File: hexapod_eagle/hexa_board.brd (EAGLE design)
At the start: 80 x 90 mm, 53 parts

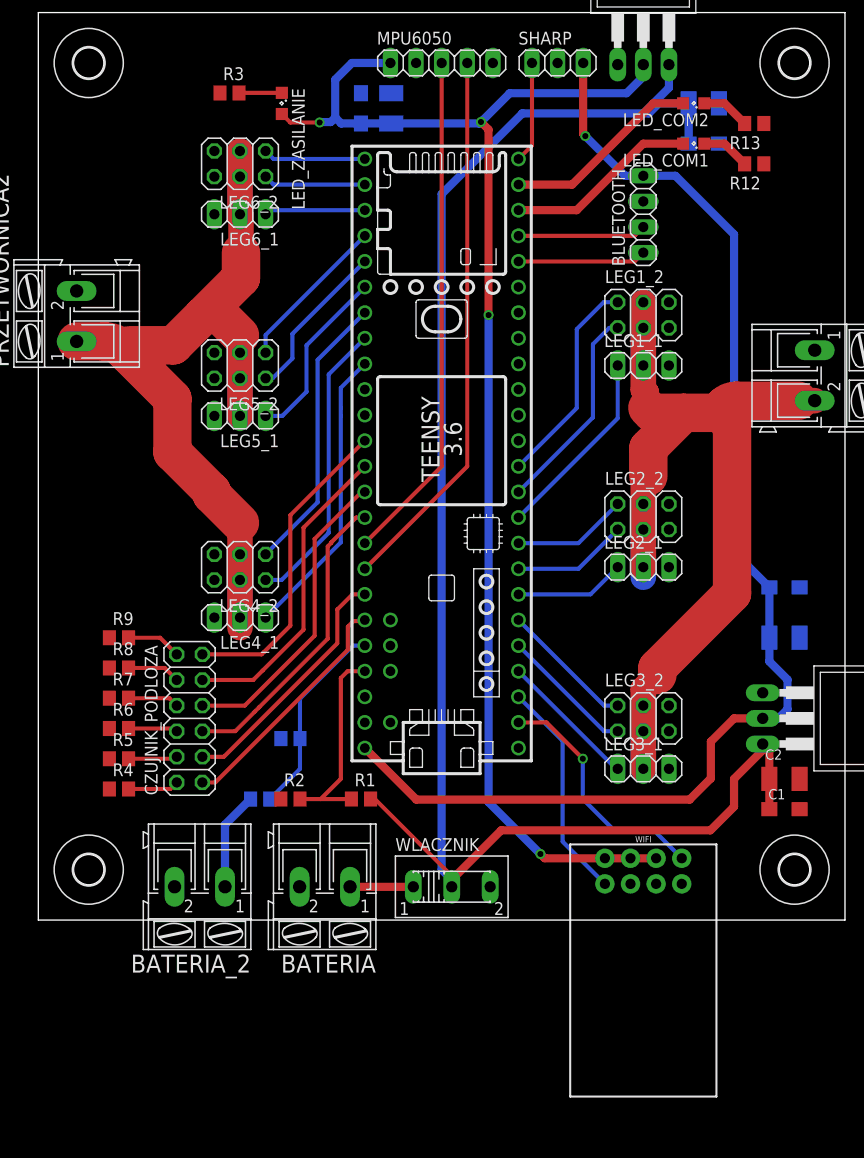
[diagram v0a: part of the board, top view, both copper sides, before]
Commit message: Update eagle files
-change to ark leg sensor pins
-change isolte value
-esp32 cam-insted bluetooth/"wifi"
-some minor changes
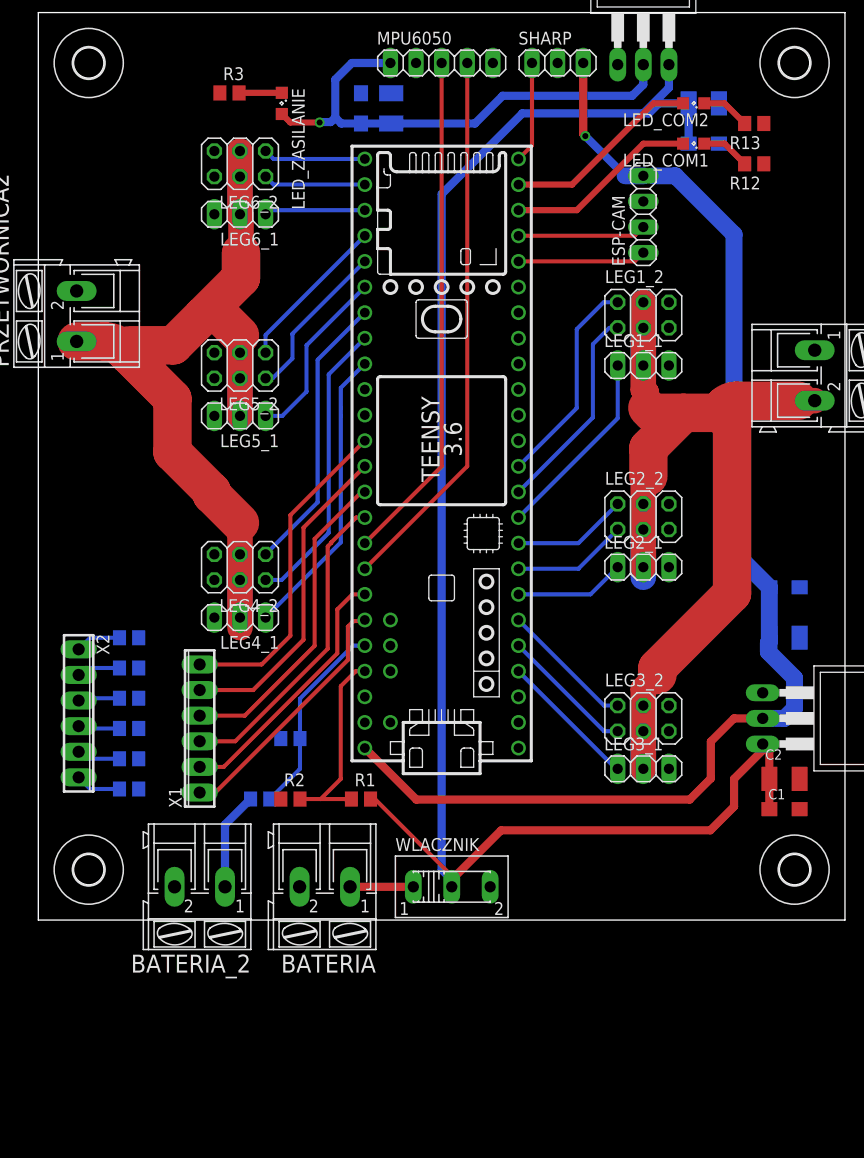
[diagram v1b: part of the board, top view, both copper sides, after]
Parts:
- removed CZUJNIK_PODLOZA: (no value), pinhead:2X06
- removed WIFI: ESP8266_ESP-01, SparkFun-RF:ESP8266_ESP-01
- added X1: ARK2, con-phoenix-254:6POL254
- added X2: ARK1, con-phoenix-254:6POL254
- BATERIA, WLACZNIK: value (none) -> 7.2V
- BATERIA_2: value (none) -> 11.1V
- ESP-CAM: value (none) -> ESP
- LED_COM1: value (none) -> YELLOW
- LED_COM2: value (none) -> RED
- LED_ZASILANIE: value (none) -> GREEN
- MPU6050: value (none) -> 6EOF
- PRZETWORNICA1, PRZETWORNICA2: value (none) -> 6V
- SHARP: value (none) -> 40CM
- moved R4 1.00 mm to (-31.0, -32.0), flipped to the bottom
- moved R5 1.00 mm to (-31.0, -29.0), flipped to the bottom
- moved R6 1.00 mm to (-31.0, -26.0), flipped to the bottom
- moved R7 1.00 mm to (-31.0, -23.0), flipped to the bottom
- moved R8 1.00 mm to (-31.0, -20.0), flipped to the bottom
- moved R9 1.00 mm to (-31.0, -17.0), flipped to the bottom
- renumbered BLUETOOTH to ESP-CAM
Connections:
- removed net INT: MPU6050.5
- removed net RXD: TEENSY41.0/RX, WIFI.1
- removed net TXD: TEENSY41.1/TX, WIFI.5
- net +3V3: no longer WIFI.2, WIFI.3, WIFI.4
- net GND: no longer WIFI.8
- net LEG1: now also X1.1; no longer CZUJNIK_PODLOZA.1
- net LEG2: now also X1.2; no longer CZUJNIK_PODLOZA.3
- net LEG3: now also X1.3; no longer CZUJNIK_PODLOZA.5
- net LEG4: now also X1.4; no longer CZUJNIK_PODLOZA.7
- net LEG5: now also X1.5; no longer CZUJNIK_PODLOZA.9
- net LEG6: now also X1.6; no longer CZUJNIK_PODLOZA.11
- net N$1: now also X2.6; no longer CZUJNIK_PODLOZA.2
- net N$2: now also X2.5; no longer CZUJNIK_PODLOZA.4
- net N$3: now also X2.4; no longer CZUJNIK_PODLOZA.6
- net N$5: now also X2.3; no longer CZUJNIK_PODLOZA.8
- net N$6: now also X2.2; no longer CZUJNIK_PODLOZA.10
- net N$7: now also X2.1; no longer CZUJNIK_PODLOZA.12
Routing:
- net +3V3: track 136.4 -> 50.1 mm, vias 4 -> 1
- net RXD: track 24.1 -> 0.00 mm, vias 1 -> 0
- net TXD: track 22.1 -> 0.00 mm
- net LEG5: track 30.8 -> 32.1 mm
- net LEG6: track 31.3 -> 32.6 mm
- net LEG3: track 30.3 -> 31.5 mm
- net LEG2: track 24.7 -> 26.0 mm
- net LEG1: track 24.1 -> 25.4 mm
- net LEG4: track 30.5 -> 31.8 mm
- net +5V: track 125.3 -> 126.3 mm
- net N$6: track 5.27 -> 4.34 mm
- net N$7: track 5.46 -> 4.53 mm
- net N$5: track 5.08 -> 4.15 mm
- net N$3: track 4.89 -> 4.15 mm
- net N$2: track 4.86 -> 4.34 mm
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
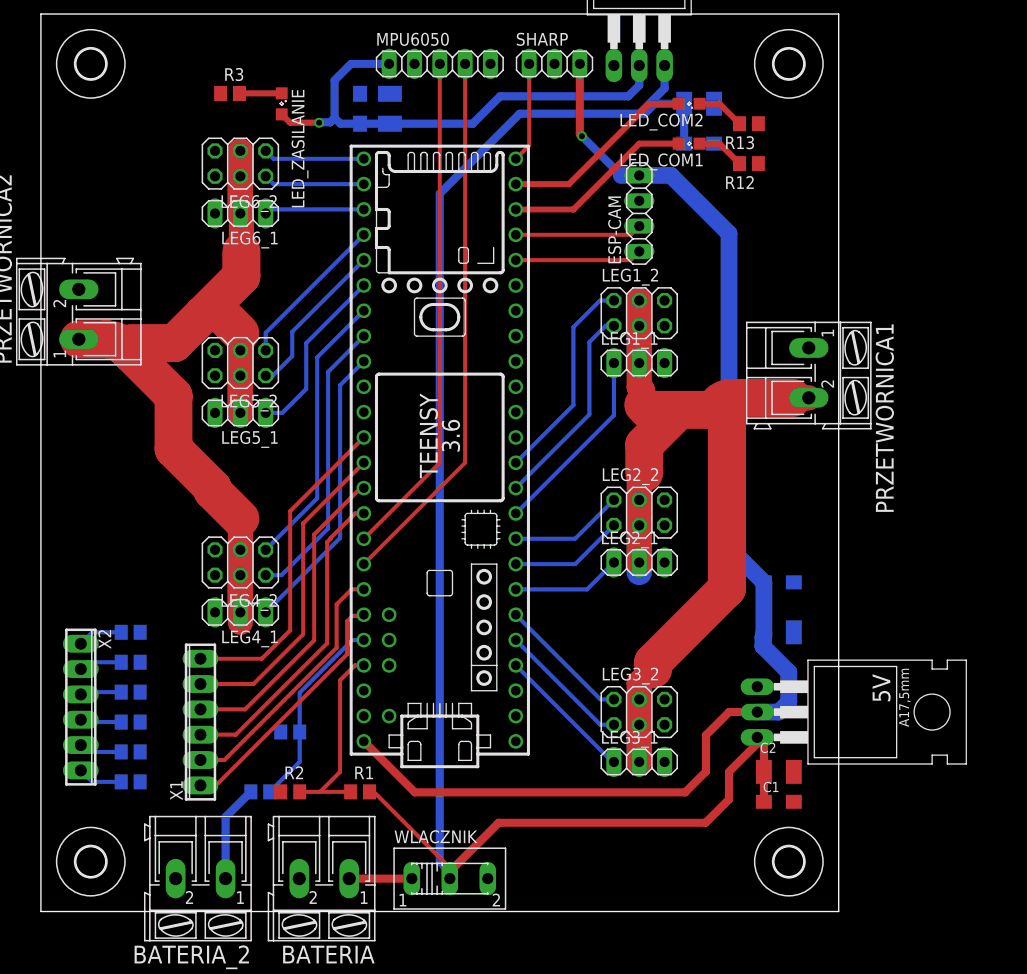
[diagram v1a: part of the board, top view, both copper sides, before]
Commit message: Update eagle schematic and board
-added capacitors
-added voltage divider
-change package some capacitors
-added on/off swich for power mcu
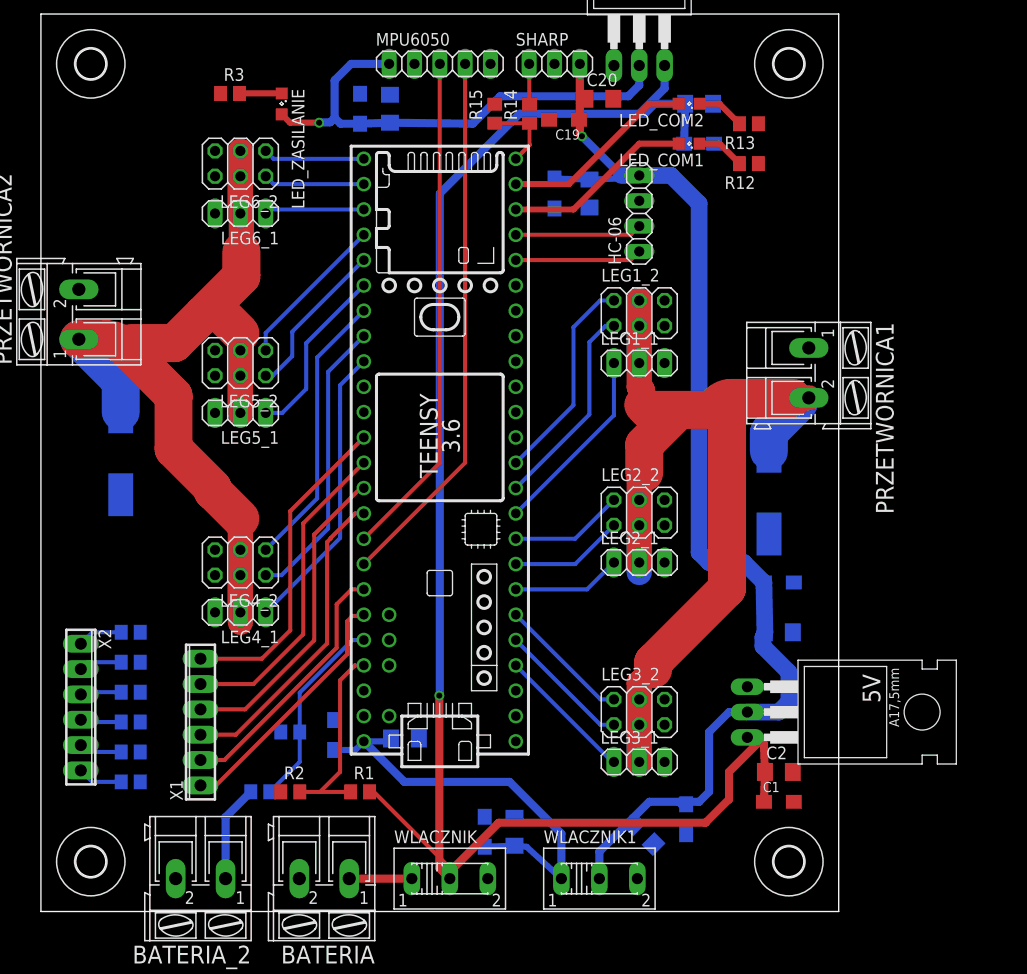
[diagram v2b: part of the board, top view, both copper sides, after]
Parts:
- added C11, C14, C15, C18, C19: 100n, rcl:SMC_A
- added C12, C13, C16, C17, C20: 10uF, rcl:C1206
- added C5, C6: (no value), rcl:150CLZ-1014
- added R14, R15: 510r, rcl:R0805
- added WLACZNIK1: 7.2V, switch:255SB
- C2, C3, C7, C8: device rcl:SMC_B -> rcl:C1206
- HC-06: value ESP -> (none)
- moved 5V 1.00 mm to (41.0, -25.0)
- renumbered ESP-CAM to HC-06
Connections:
- new net +5MCU: C11.+, C12.1, C13.1, C14.+, TEENSY41.VIN, WLACZNIK1.1
- new net N$10: R14.2, SHARP.1
- net +3V3: now also C8.1; no longer C8.+
- net +5V: now also C15.+, C16.1, C17.1, C18.+, C19.+, C20.1, C3.1, WLACZNIK1.2; no longer C3.+, TEENSY41.VIN
- net +6V1: now also C5.+
- net +6V2: now also C6.+
- net +BAT: now also C2.1, C7.1; no longer C2.+, C7.+
- net GND: now also C11.-, C12.2, C13.2, C14.-, C15.-, C16.2, C17.2, C18.-, C19.-, C2.2, C20.2, C3.2, C5.-, C6.-, C7.2, C8.2, R15.2; no longer C2.-, C3.-, C7.-, C8.-
- net SENSOR: now also R14.1, R15.1; no longer SHARP.1
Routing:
- net +5MCU: track 0.00 -> 43.2 mm
- net +6V2: track 95.6 -> 104.7 mm
- net +5V: track 126.3 -> 118.7 mm
- net +6V1: track 140.7 -> 146.8 mm
- net N$10: track 0.00 -> 4.07 mm
- net SENSOR: track 10.1 -> 7.64 mm
- net +BAT: track 164.6 -> 166.2 mm, vias 0 -> 1
